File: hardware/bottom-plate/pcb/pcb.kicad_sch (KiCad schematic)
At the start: 66 parts, among them SW1 MT-0-102-A101-M200-RS+PJ, SW2 TS4535TP 250GF 009, SW3 TS4535TP 250GF 009

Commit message: some misc bottom plate changes
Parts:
- MCU1: footprint RP-Pico Libraries:RPi_Pico_SMD_TH_USBC_cable_cutout -> RP-Pico Libraries:RPi_Pico_SMD_TH
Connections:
- net +3V3: now also JP4.1 (A), JP8.1 (A); no longer JP4.3 (B), JP8.3 (B)
- net GND: now also JP4.3 (B), JP8.3 (B); no longer JP4.1 (A), JP8.1 (A)
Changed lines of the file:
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@@
 	)
 	(symbol
-		(lib_name "Jumper_3_Bridged12_1")
 		(lib_id "Jumper:Jumper_3_Bridged12")
 		(at 294.64 64.77 180)
@@
 	)
 	(symbol
-		(lib_name "Jumper_3_Bridged12_1")
 		(lib_id "Jumper:Jumper_3_Bridged12")
 		(at 69.85 162.56 0)
@@
 			)
 		)
-		(property "Footprint" "RP-Pico Libraries:RPi_Pico_SMD_TH_USBC_cable_cutout"
+		(property "Footprint" "RP-Pico Libraries:RPi_Pico_SMD_TH"
 			(at 204.47 237.49 90)
 			(effects
@@
 	)
 	(symbol
-		(lib_name "MCP23S17_SO_1")
 		(lib_id "Interface_Expansion:MCP23S17_SO")
 		(at 154.94 81.28 0)

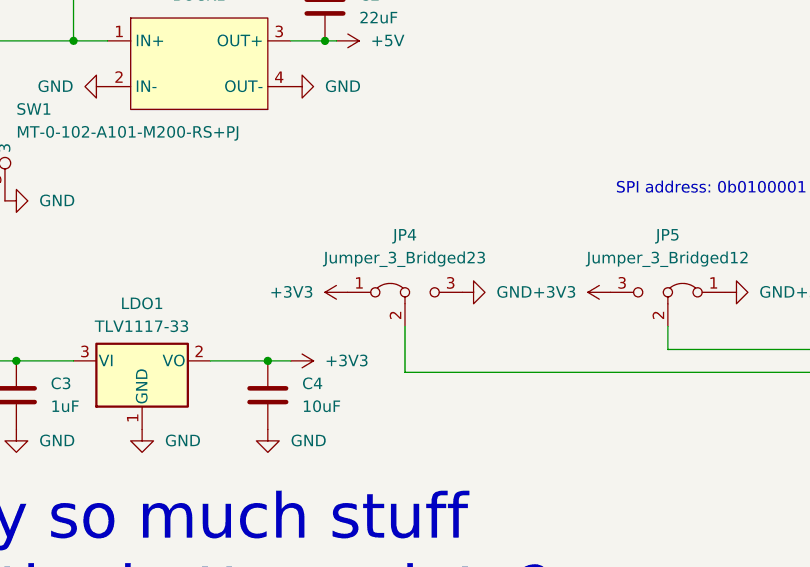
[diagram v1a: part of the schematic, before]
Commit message: fixed up bottom plate schematic. do not run a global symbol update! all modified symbols as of now are intentionally modified locally.
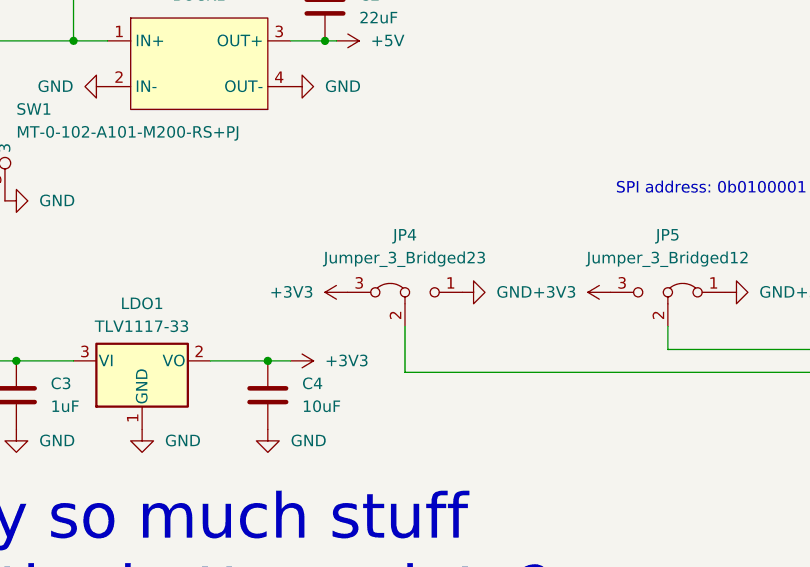
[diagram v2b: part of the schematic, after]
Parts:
- MCU1: footprint RP-Pico Libraries:RPi_Pico_SMD_TH -> RP-Pico Libraries:RPi_Pico_SMD_TH_USBC_cable_cutout
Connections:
- net +3V3: now also JP4.3 (A); no longer JP4.1 (A)
- net GND: now also JP4.1 (B); no longer JP4.3 (B)
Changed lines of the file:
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@@
 	)
 	(symbol
+		(lib_name "Jumper_3_Bridged12_1")
 		(lib_id "Jumper:Jumper_3_Bridged12")
 		(at 69.85 162.56 0)
@@
 	)
 	(symbol
+		(lib_name "MCP23S17_SO_1")
 		(lib_id "Interface_Expansion:MCP23S17_SO")
 		(at 154.94 151.13 0)
@@
 			)
 		)
-		(property "Footprint" "RP-Pico Libraries:RPi_Pico_SMD_TH"
+		(property "Footprint" "RP-Pico Libraries:RPi_Pico_SMD_TH_USBC_cable_cutout"
 			(at 204.47 237.49 90)
 			(effects

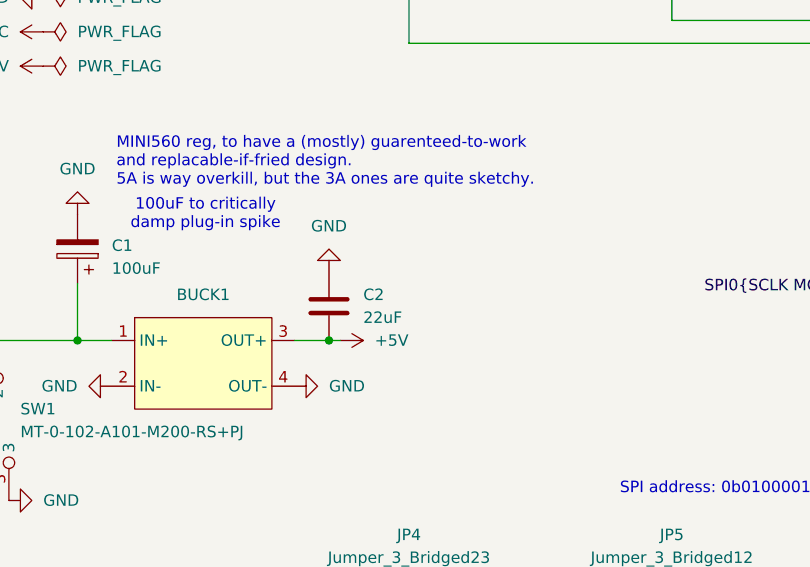
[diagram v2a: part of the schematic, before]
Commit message: added fuse to bottom plate
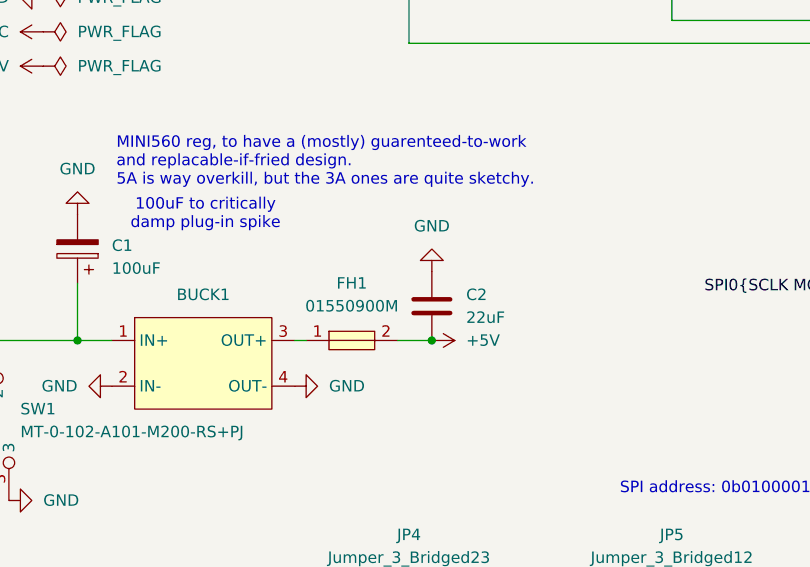
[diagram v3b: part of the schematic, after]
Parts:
- added FH1: 01550900M, EasyEDA:FUSE-SMD_L9.8-W5.0, symbol EasyEDA:01550900M
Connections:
- net +5V: now also FH1.2; no longer BUCK1.3 (OUT+)
- new net: BUCK1.3 (OUT+), FH1.1
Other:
- moved on the sheet: C2
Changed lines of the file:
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@@
 	)
 	(junction
-		(at 60.96 134.62)
+		(at 193.04 170.18)
 		(diameter 0)
 		(color 0 0 0 0)
 	)
 	(junction
-		(at 193.04 170.18)
+		(at 72.39 134.62)
 		(diameter 0)
 		(color 0 0 0 0)
@@
 	(wire
 		(pts
+			(xy 68.58 134.62) (xy 72.39 134.62)
+		)
+		(stroke
+			(width 0)
+			(type default)
+		)
+	)
+	(wire
+		(pts
 			(xy 220.98 180.34) (xy 241.3 180.34)
 		)
@@
 	(wire
 		(pts
-			(xy 62.23 134.62) (xy 60.96 134.62)
-		)
-		(stroke
-			(width 0)
-			(type default)
-		)
-	)
-	(wire
-		(pts
 			(xy 300.99 179.07) (xy 311.15 179.07)
 		)
@@
 	(wire
 		(pts
-			(xy 60.96 134.62) (xy 57.15 134.62)
-		)
-		(stroke
-			(width 0)
-			(type default)
-		)
-	)
-	(wire
-		(pts
 			(xy 335.28 74.93) (xy 345.44 74.93)
 		)
@@
 	(wire
 		(pts
+			(xy 57.15 134.62) (xy 58.42 134.62)
+		)
+		(stroke
+			(width 0)
+			(type default)
+		)
+	)
+	(wire
+		(pts
 			(xy 125.73 133.35) (xy 137.16 133.35)
 		)
@@
 	)
 	(symbol
-		(lib_id "Mechanical:MountingHole_Pad")
-		(at 41.91 236.22 90)
+		(lib_id "power:+5V")
+		(at 72.39 134.62 270)
+		(mirror x)
 		(unit 1)
-		(exclude_from_sim yes)
-		(in_bom no)
+		(exclude_from_sim no)
+		(in_bom yes)
 		(on_board yes)
 		(dnp no)
 		(fields_autoplaced yes)
-		(property "Reference" "H2"
-			(at 40.64 229.87 90)
+		(property "Reference" "#PWR019"
+			(at 68.58 134.62 0)
 			(effects
 				(font
 					(size 1.27 1.27)
 				)
+				(hide yes)
 			)
 		)
-		(property "Value" "MountingHole_Pad"
-			(at 40.64 232.41 90)
+		(property "Value" "+5V"
+			(at 76.2 134.6199 90)
 			(effects
 				(font
 					(size 1.27 1.27)
 				)
+				(justify left)
 			)
 		)
-		(property "Footprint" "MountingHole:MountingHole_3.2mm_M3_Pad_Via"
-			(at 41.91 236.22 0)
+		(property "Footprint" ""
+			(at 72.39 134.62 0)
 			(effects
 				(font
@@
 			)
 		)
-		(property "Datasheet" "~"
-			(at 41.91 236.22 0)
+		(property "Datasheet" ""
+			(at 72.39 134.62 0)
 			(effects
 				(font
@@
 			)
 		)
-		(property "Description" "Mounting Hole with connection"
-			(at 41.91 236.22 0)
+		(property "Description" "Power symbol creates a global label with name \"+5V\""
+			(at 72.39 134.62 0)
 			(effects
 				(font
@@
 			(project "pcb"
 				(path "/7e6d4b79-c480-4b70-bccc-d28260cddf7c"
-					(reference "H2")
+					(reference "#PWR019")
 					(unit 1)
 				)
@@
 	)
 	(symbol
-		(lib_id "power:GND")
-		(at 336.55 224.79 0)
+		(lib_id "Mechanical:MountingHole_Pad")
+		(at 41.91 236.22 90)
 		(unit 1)
-		(exclude_from_sim no)
-		(in_bom yes)
+		(exclude_from_sim yes)
+		(in_bom no)
 		(on_board yes)
 		(dnp no)
 		(fields_autoplaced yes)
-		(property "Reference" "#PWR077"
-			(at 336.55 231.14 0)
+		(property "Reference" "H2"
+			(at 40.64 229.87 90)
 			(effects
 				(font
 					(size 1.27 1.27)
 				)
-				(hide yes)
 			)
 		)
-		(property "Value" "GND"
-			(at 336.55 229.87 0)
+		(property "Value" "MountingHole_Pad"
+			(at 40.64 232.41 90)
 			(effects
 				(font
@@
 			)
 		)
-		(property "Footprint" ""
-			(at 336.55 224.79 0)
+		(property "Footprint" "MountingHole:MountingHole_3.2mm_M3_Pad_Via"
+			(at 41.91 236.22 0)
 			(effects
 				(font
@@
 			)
 		)
-		(property "Datasheet" ""
-			(at 336.55 224.79 0)
+		(property "Datasheet" "~"
+			(at 41.91 236.22 0)
 			(effects
 				(font
@@
 			)
 		)
-		(property "Description" "Power symbol creates a global label with name \"GND\" , ground"
-			(at 336.55 224.79 0)
+		(property "Description" "Mounting Hole with connection"
+			(at 41.91 236.22 0)
 			(effects
 				(font
@@
 			(project "pcb"
 				(path "/7e6d4b79-c480-4b70-bccc-d28260cddf7c"
-					(reference "#PWR077")
+					(reference "H2")
 					(unit 1)
 				)
@@
 	)
 	(symbol
-		(lib_id "power:+5V")
-		(at 62.23 134.62 270)
-		(mirror x)
+		(lib_id "power:GND")
+		(at 336.55 224.79 0)
 		(unit 1)
 		(exclude_from_sim no)
@@
 		(dnp no)
 		(fields_autoplaced yes)
-		(property "Reference" "#PWR019"
-			(at 58.42 134.62 0)
+		(property "Reference" "#PWR077"
+			(at 336.55 231.14 0)
 			(effects
 				(font
@@
 			)
 		)
-		(property "Value" "+5V"
-			(at 66.04 134.6199 90)
+		(property "Value" "GND"
+			(at 336.55 229.87 0)
 			(effects
 				(font
 					(size 1.27 1.27)
 				)
-				(justify left)
 			)
 		)
 		(property "Footprint" ""
-			(at 62.23 134.62 0)
+			(at 336.55 224.79 0)
 			(effects
 				(font
@@
 		)
 		(property "Datasheet" ""
-			(at 62.23 134.62 0)
+			(at 336.55 224.79 0)
 			(effects
 				(font
@@
 			)
 		)
-		(property "Description" "Power symbol creates a global label with name \"+5V\""
-			(at 62.23 134.62 0)
+		(property "Description" "Power symbol creates a global label with name \"GND\" , ground"
+			(at 336.55 224.79 0)
 			(effects
 				(font
@@
 			(project "pcb"
 				(path "/7e6d4b79-c480-4b70-bccc-d28260cddf7c"
-					(reference "#PWR019")
+					(reference "#PWR077")
 					(unit 1)
 				)
@@
 	)
 	(symbol
+		(lib_id "EasyEDA:01550900M")
+		(at 63.5 134.62 0)
+		(unit 1)
+		(exclude_from_sim no)
+		(in_bom yes)
+		(on_board yes)
+		(dnp no)
+		(fields_autoplaced yes)
+		(property "Reference" "FH1"
+			(at 63.5 128.27 0)
+			(effects
+				(font
+					(size 1.27 1.27)
+				)
+			)
+		)
+		(property "Value" "01550900M"
+			(at 63.5 130.81 0)
+			(effects
+				(font
+					(size 1.27 1.27)
+				)
+			)
+		)
+		(property "Footprint" "EasyEDA:FUSE-SMD_L9.8-W5.0"
+			(at 63.5 142.24 0)
+			(effects
+				(font
+					(size 1.27 1.27)
+				)
+				(hide yes)
+			)
+		)
+		(property "Datasheet" "https://lcsc.com/product-detail/Others_Littelfuse_01550900M_Littelfuse-01550900M_C108518.html"
+			(at 63.5 144.78 0)
+			(effects
+				(font
+					(size 1.27 1.27)
+				)
+				(hide yes)
+			)
+		)
+		(property "Description" ""
+			(at 63.5 134.62 0)
+			(effects
+				(font
+					(size 1.27 1.27)
+				)
+				(hide yes)
+			)
+		)
+		(property "LCSC Part" "C108518"
+			(at 63.5 147.32 0)
+			(effects
+				(font
+					(size 1.27 1.27)
+				)
+				(hide yes)
+			)
+		)
+		(pin "2"
+		)
+		(pin "1"
+		)
+		(instances
+			(project "pcb"
+				(path "/7e6d4b79-c480-4b70-bccc-d28260cddf7c"
+					(reference "FH1")
+					(unit 1)
+				)
+			)
+		)
+	)
+	(symbol
 		(lib_id "power:GND")
 		(at 57.15 139.7 90)
@@
 	(symbol
 		(lib_id "power:GND")
-		(at 60.96 127 180)
+		(at 72.39 127 180)
 		(unit 1)
 		(exclude_from_sim no)
@@
 		(fields_autoplaced yes)
 		(property "Reference" "#PWR017"
-			(at 60.96 120.65 0)
+			(at 72.39 120.65 0)
 			(effects
 				(font
@@
 		)
 		(property "Value" "GND"
-			(at 60.96 121.92 0)
+			(at 72.39 121.92 0)
 			(effects
 				(font
@@
 		)
 		(property "Footprint" ""
-			(at 60.96 127 0)
+			(at 72.39 127 0)
 			(effects
 				(font
@@
 		)
 		(property "Datasheet" ""
-			(at 60.96 127 0)
+			(at 72.39 127 0)
 			(effects
 				(font
@@
 		)
 		(property "Description" "Power symbol creates a global label with name \"GND\" , ground"
-			(at 60.96 127 0)
+			(at 72.39 127 0)
 			(effects
 				(font
@@
 	(symbol
 		(lib_id "Device:C")
-		(at 60.96 130.81 0)
+		(at 72.39 130.81 0)
 		(mirror y)
 		(unit 1)
@@
 		(fields_autoplaced yes)
 		(property "Reference" "C2"
-			(at 64.77 129.5399 0)
+			(at 76.2 129.5399 0)
 			(effects
 				(font
@@
 		)
 		(property "Value" "22uF"
-			(at 64.77 132.0799 0)
+			(at 76.2 132.0799 0)
 			(effects
 				(font
@@
 		)
 		(property "Footprint" "PCM_Capacitor_SMD_AKL:C_0805_2012Metric_Pad1.15x1.40mm_HandSolder"
-			(at 59.9948 134.62 0)
+			(at 71.4248 134.62 0)
 			(effects
 				(font
@@
 		)
 		(property "Datasheet" "~"
-			(at 60.96 130.81 0)
+			(at 72.39 130.81 0)
 			(effects
 				(font
@@
 		)
 		(property "Description" "Unpolarized capacitor"
-			(at 60.96 130.81 0)
+			(at 72.39 130.81 0)
 			(effects
 				(font
